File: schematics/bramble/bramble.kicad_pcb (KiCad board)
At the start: 2 copper layers, 6 parts, among them Q1 IRLB8721PBF, Q2 IRLB8721PBF, Q3 IRF9540N, Q4 IRF9540N, Q5 IRLB8721PBF, Q6 IRLB8721PBF

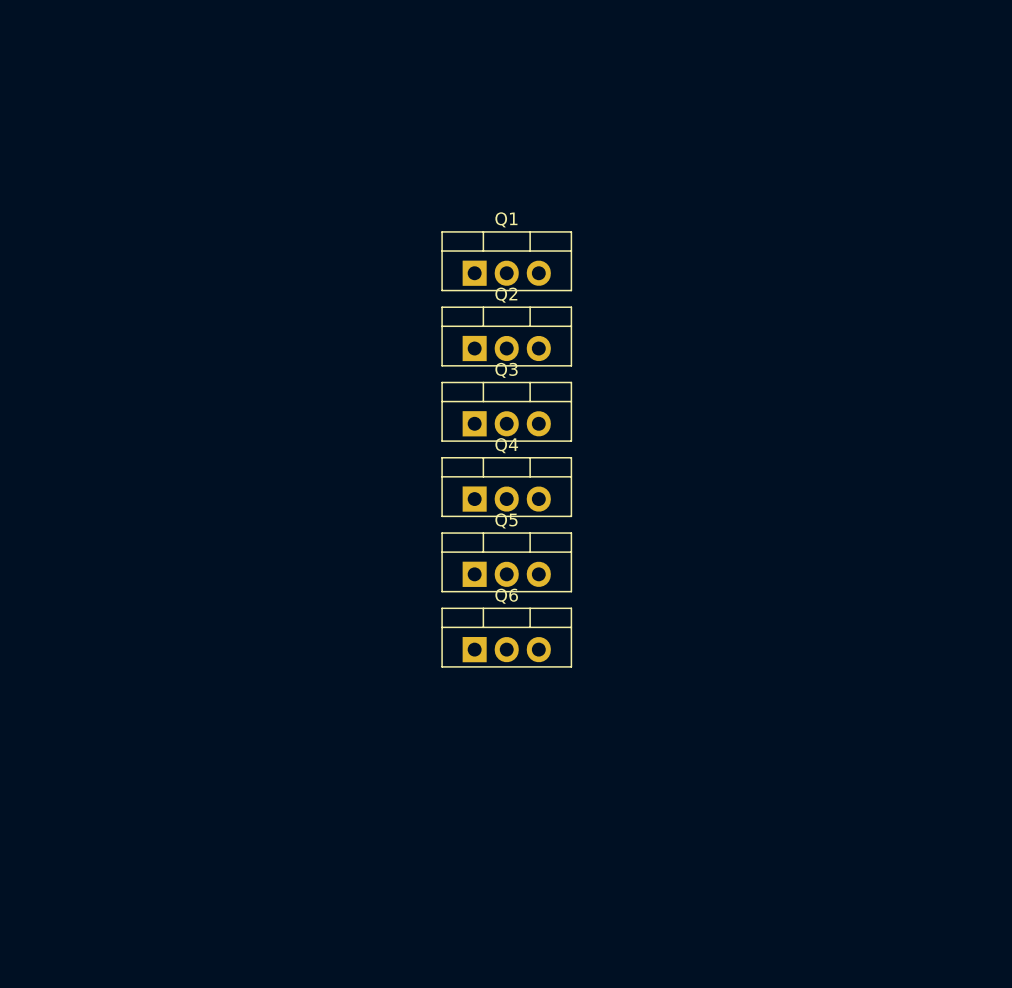
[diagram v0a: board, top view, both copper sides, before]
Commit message: Shematics: split out valve indexer, copy design from rp2040 feather
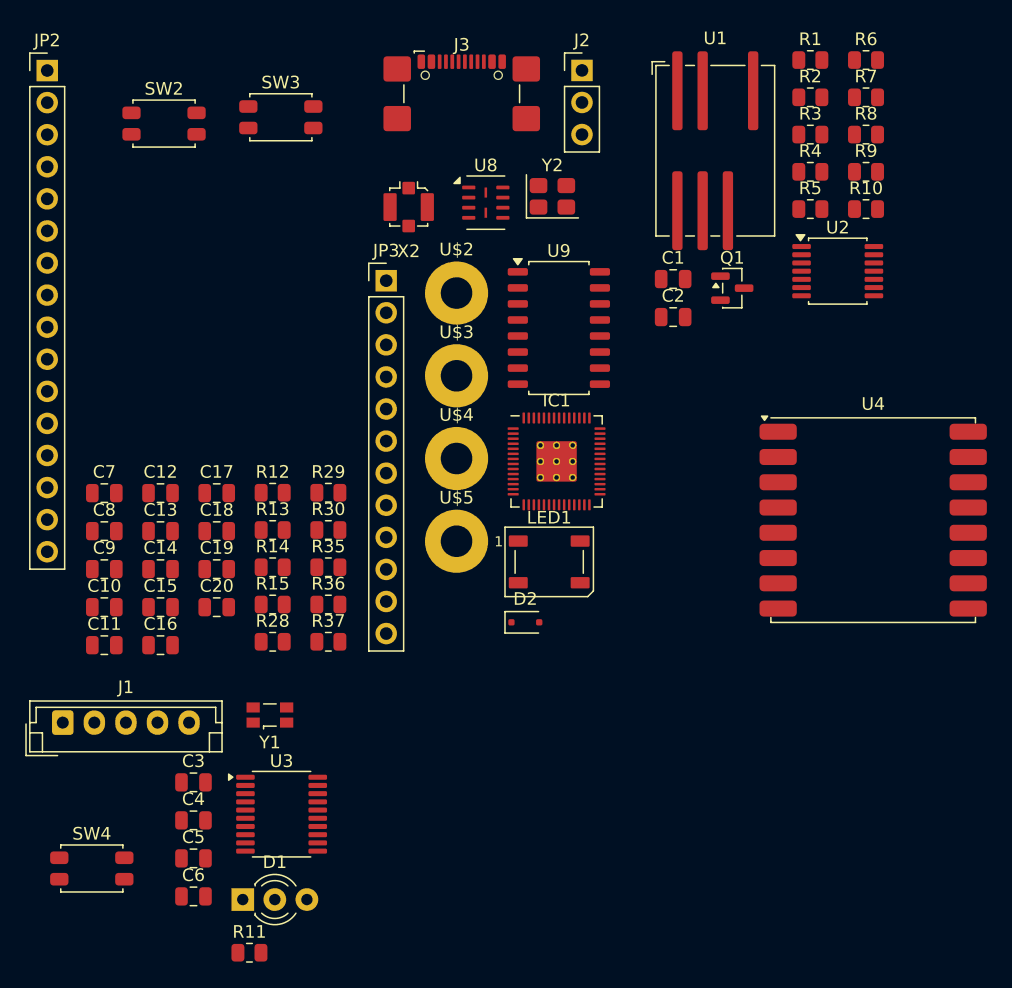
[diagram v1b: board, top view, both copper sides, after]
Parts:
- removed Q2, Q5, Q6: IRLB8721PBF, Package_TO_SOT_THT:TO-220-3_Vertical
- removed Q3, Q4: IRF9540N, Package_TO_SOT_THT:TO-220-3_Vertical
- added C1: 10uF, Capacitor_SMD:C_0805_2012Metric, F.Cu at (81.1, 45.7)
- added C10: 22pF, Capacitor_SMD:C_0805_2012Metric, F.Cu at (36.1, 71.6)
- added C11: 0.1uF, Capacitor_SMD:C_0805_2012Metric, F.Cu at (36.1, 74.7)
- added C12: 0.1uF, Capacitor_SMD:C_0805_2012Metric, F.Cu at (40.5, 62.6)
- added C13: 1uF, Capacitor_SMD:C_0805_2012Metric, F.Cu at (40.5, 65.6)
- added C14: 1uF, Capacitor_SMD:C_0805_2012Metric, F.Cu at (40.5, 68.6)
- added C15: 0.1uF, Capacitor_SMD:C_0805_2012Metric, F.Cu at (40.5, 71.6)
- added C16: 1uF, Capacitor_SMD:C_0805_2012Metric, F.Cu at (40.5, 74.7)
- added C17: 0.1uF, Capacitor_SMD:C_0805_2012Metric, F.Cu at (45.0, 62.6)
- added C18: 0.1uF, Capacitor_SMD:C_0805_2012Metric, F.Cu at (45.0, 65.6)
- added C19: 0.1uF, Capacitor_SMD:C_0805_2012Metric, F.Cu at (45.0, 68.6)
- added C2: 10uF, Capacitor_SMD:C_0805_2012Metric, F.Cu at (81.1, 48.7)
- added C20: 1uF, Capacitor_SMD:C_0805_2012Metric, F.Cu at (45.0, 71.6)
- added C3: 4.7uF, Capacitor_SMD:C_0805_2012Metric, F.Cu at (43.2, 85.5)
- added C4: 100nF, Capacitor_SMD:C_0805_2012Metric, F.Cu at (43.2, 88.5)
- added C5: 100nF, Capacitor_SMD:C_0805_2012Metric, F.Cu at (43.2, 91.5)
- added C6: 100nF, Capacitor_SMD:C_0805_2012Metric, F.Cu at (43.2, 94.5)
- added C7: 0.1uF, Capacitor_SMD:C_0805_2012Metric, F.Cu at (36.1, 62.6)
- added C8: 1uF, Capacitor_SMD:C_0805_2012Metric, F.Cu at (36.1, 65.6)
- added C9: 22pF, Capacitor_SMD:C_0805_2012Metric, F.Cu at (36.1, 68.6)
- added D1: LED_Dual_AKA, LED_THT:LED_D3.0mm-3, F.Cu at (47.1, 94.8)
- added D2: 1N4148, Diode_SMD:D_SOD-323F, F.Cu at (69.4, 72.8)
- added IC1: RP2040_QFN56, RP2040:RP2040-QFN-56, F.Cu at (71.9, 60.1)
- added J1: Conn_01x05_Pin, Connector_JST:JST_EH_B5B-EH-A_1x05_P2.50mm_Vertical, F.Cu at (32.8, 80.8)
- added J2: Conn_01x03, Connector_PinHeader_2.54mm:PinHeader_1x03_P2.54mm_Vertical, F.Cu at (73.9, 29.1)
- added J3: USB_C_Receptacle_USB2.0_16P, Connector_USB:USB_C_Receptacle_GCT_USB4110, F.Cu at (64.4, 32.1)
- added JP2: HEADER-1X16ROUND, Connector_PinHeader_2.54mm:PinHeader_1x16_P2.54mm_Vertical, F.Cu at (31.6, 29.1)
- added JP3: HEADER-1X12, Connector_PinHeader_2.54mm:PinHeader_1x12_P2.54mm_Vertical, F.Cu at (58.4, 45.8)
- added LED1: WS2812B_SK6805_1515, LED_SMD:LED_WS2812B_PLCC4_5.0x5.0mm_P3.2mm, F.Cu at (71.3, 68.1)
- added R1: 100, Resistor_SMD:R_0805_2012Metric, F.Cu at (92.0, 28.3)
- added R10: 8.2k, Resistor_SMD:R_0805_2012Metric, F.Cu at (96.4, 40.1)
- added R11: 10k, Resistor_SMD:R_0805_2012Metric, F.Cu at (47.6, 99.0)
- added R12: 5.1K, Resistor_SMD:R_0805_2012Metric, F.Cu at (49.4, 62.6)
- added R13: 5.1K, Resistor_SMD:R_0805_2012Metric, F.Cu at (49.4, 65.5)
- added R14: 22 ohm, Resistor_SMD:R_0805_2012Metric, F.Cu at (49.4, 68.5)
- added R15: 22 ohm, Resistor_SMD:R_0805_2012Metric, F.Cu at (49.4, 71.4)
- added R2: 10k, Resistor_SMD:R_0805_2012Metric, F.Cu at (92.0, 31.3)
- added R28: 10K, Resistor_SMD:R_0805_2012Metric, F.Cu at (49.4, 74.4)
- added R29: 1K, Resistor_SMD:R_0805_2012Metric, F.Cu at (53.8, 62.6)
- added R3: 1k, Resistor_SMD:R_0805_2012Metric, F.Cu at (92.0, 34.2)
- added R30: 1K, Resistor_SMD:R_0805_2012Metric, F.Cu at (53.8, 65.5)
- added R35: 10K, Resistor_SMD:R_0805_2012Metric, F.Cu at (53.8, 68.5)
- added R36: 10K, Resistor_SMD:R_0805_2012Metric, F.Cu at (53.8, 71.4)
- added R37: 10K, Resistor_SMD:R_0805_2012Metric, F.Cu at (53.8, 74.4)
- added R4: 100, Resistor_SMD:R_0805_2012Metric, F.Cu at (92.0, 37.2)
- added R5: 1k, Resistor_SMD:R_0805_2012Metric, F.Cu at (92.0, 40.1)
- added R6: 0.1, Resistor_SMD:R_0805_2012Metric, F.Cu at (96.4, 28.3)
- added R7: 10k, Resistor_SMD:R_0805_2012Metric, F.Cu at (96.4, 31.3)
- added R8: 1k, Resistor_SMD:R_0805_2012Metric, F.Cu at (96.4, 34.2)
- added R9: 20k, Resistor_SMD:R_0805_2012Metric, F.Cu at (96.4, 37.2)
- added SW2: SW_MEC_5E, Button_Switch_SMD:SW_SPST_EVQP2_MiddlePushTravel_H2.5mm, F.Cu at (40.8, 33.4)
- added SW3: SW_MEC_5E, Button_Switch_SMD:SW_SPST_EVQP2_MiddlePushTravel_H2.5mm, F.Cu at (50.1, 32.9)
- added SW4: SW_MEC_5E, Button_Switch_SMD:SW_SPST_EVQP2_MiddlePushTravel_H2.5mm, F.Cu at (35.1, 92.3)
- added U$2: MOUNTINGHOLE2.5, MountingHole:MountingHole_2.5mm_Pad, F.Cu at (64.0, 46.8)
- added U$3: MOUNTINGHOLE2.5, MountingHole:MountingHole_2.5mm_Pad, F.Cu at (64.0, 53.3)
- added U$4: MOUNTINGHOLE2.5, MountingHole:MountingHole_2.5mm_Pad, F.Cu at (64.0, 59.9)
- added U$5: MOUNTINGHOLE2.5, MountingHole:MountingHole_2.5mm_Pad, F.Cu at (64.0, 66.4)
- added U1: TDN_5-0910WISM, Converter_DCDC:Converter_DCDC_TRACO_TDN_5-xxxxWISM_SMD, F.Cu at (84.5, 35.5)
- added U2: Opamp_Quad, Package_SO:TSSOP-14_4.4x5mm_P0.65mm, F.Cu at (94.2, 45.0)
- added U3: STM32L010F4P6, Package_SO:TSSOP-20_4.4x6.5mm_P0.65mm, F.Cu at (50.1, 88.0)
- added U4: RFM95W-915S2, RF_Module:HOPERF_RFM9XW_SMD, F.Cu at (97.0, 64.8)
- added U8: 8MB QSPI, Package_SON:Winbond_USON-8-2EP_3x4mm_P0.8mm_EP0.2x0.8mm, F.Cu at (66.3, 39.6)
- added U9: MT25QL01GBBB8ESF-0SIT, Package_SO:SOP-16_4.55x10.3mm_P1.27mm, F.Cu at (72.1, 49.5)
- added X2: uFL, Connector_Coaxial:U.FL_Molex_MCRF_73412-0110_Vertical, F.Cu at (60.2, 40.0)
- added Y1: SG-3030CM, Oscillator:Oscillator_SMD_SeikoEpson_SG3030CM, F.Cu at (49.2, 80.2)
- added Y2: 12Mhz, Crystal:Crystal_SMD_Abracon_ABM8G-4Pin_3.2x2.5mm, F.Cu at (71.6, 39.1)
- Q1: value IRLB8721PBF -> DMN3300U; footprint Package_TO_SOT_THT:TO-220-3_Vertical -> Package_TO_SOT_SMD:SOT-23
- moved Q1 20.4 mm to (85.8, 46.4)
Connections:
- Q1 pad 2: /M+ -> +9V
- Q1 pad 3: GND -> Net-(Q1-D)
